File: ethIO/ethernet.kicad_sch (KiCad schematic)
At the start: 40 parts, among them J7 HR911130A1, U10 RTL8211E-VB-CG, Y1 25MHz

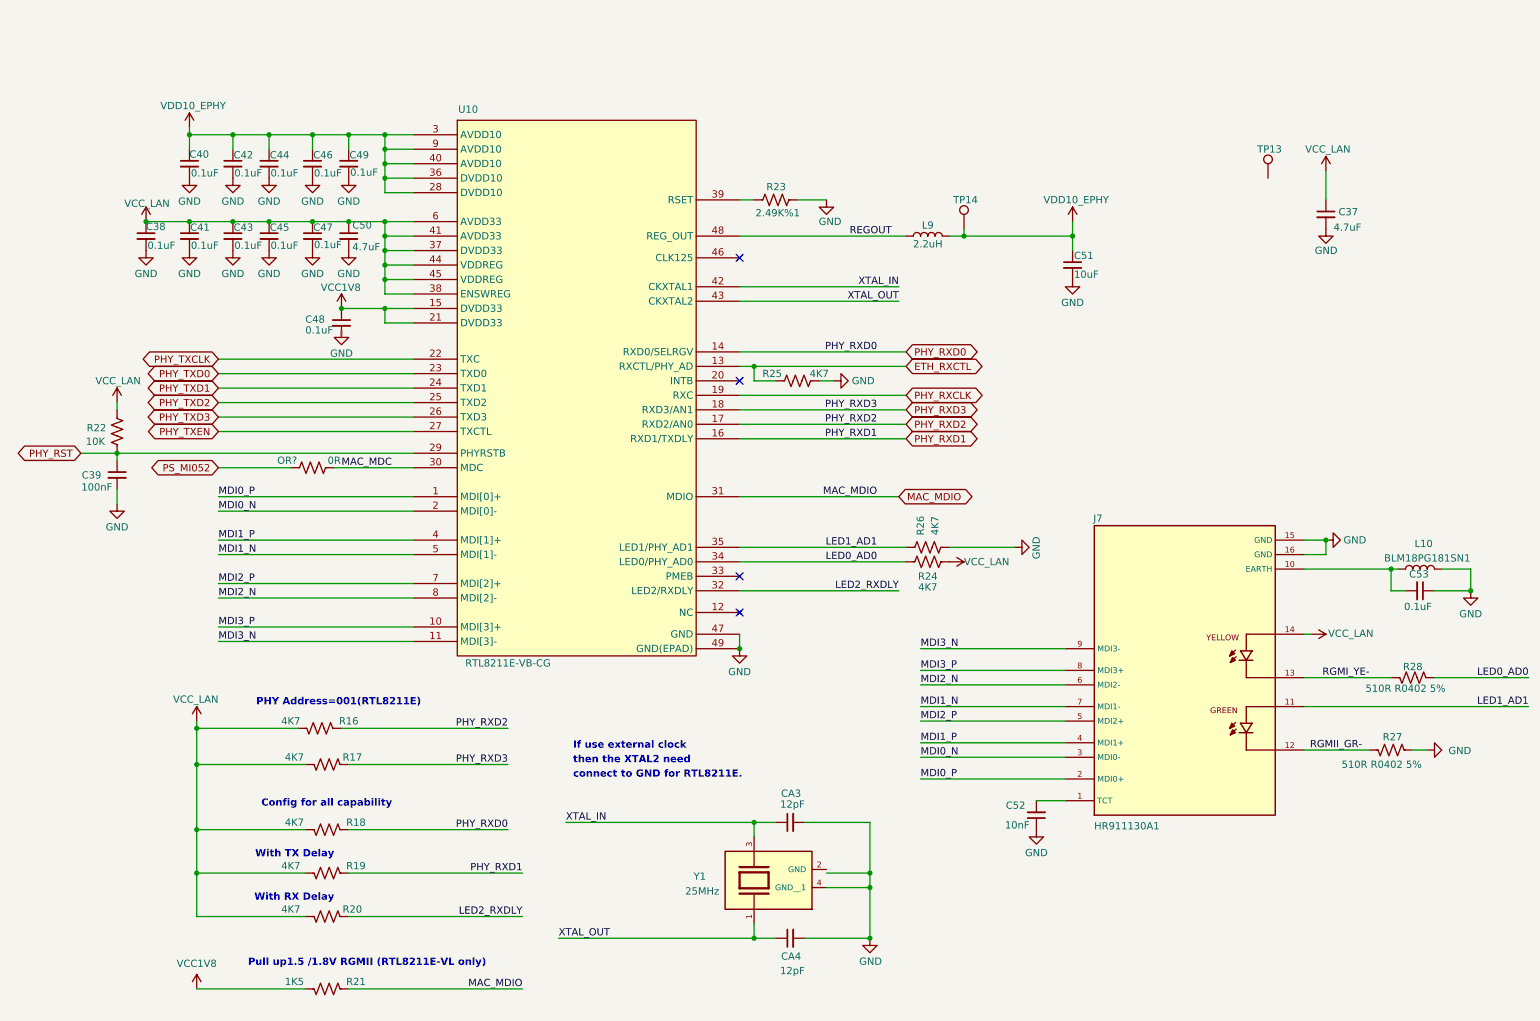
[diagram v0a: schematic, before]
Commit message: Updating ethIO
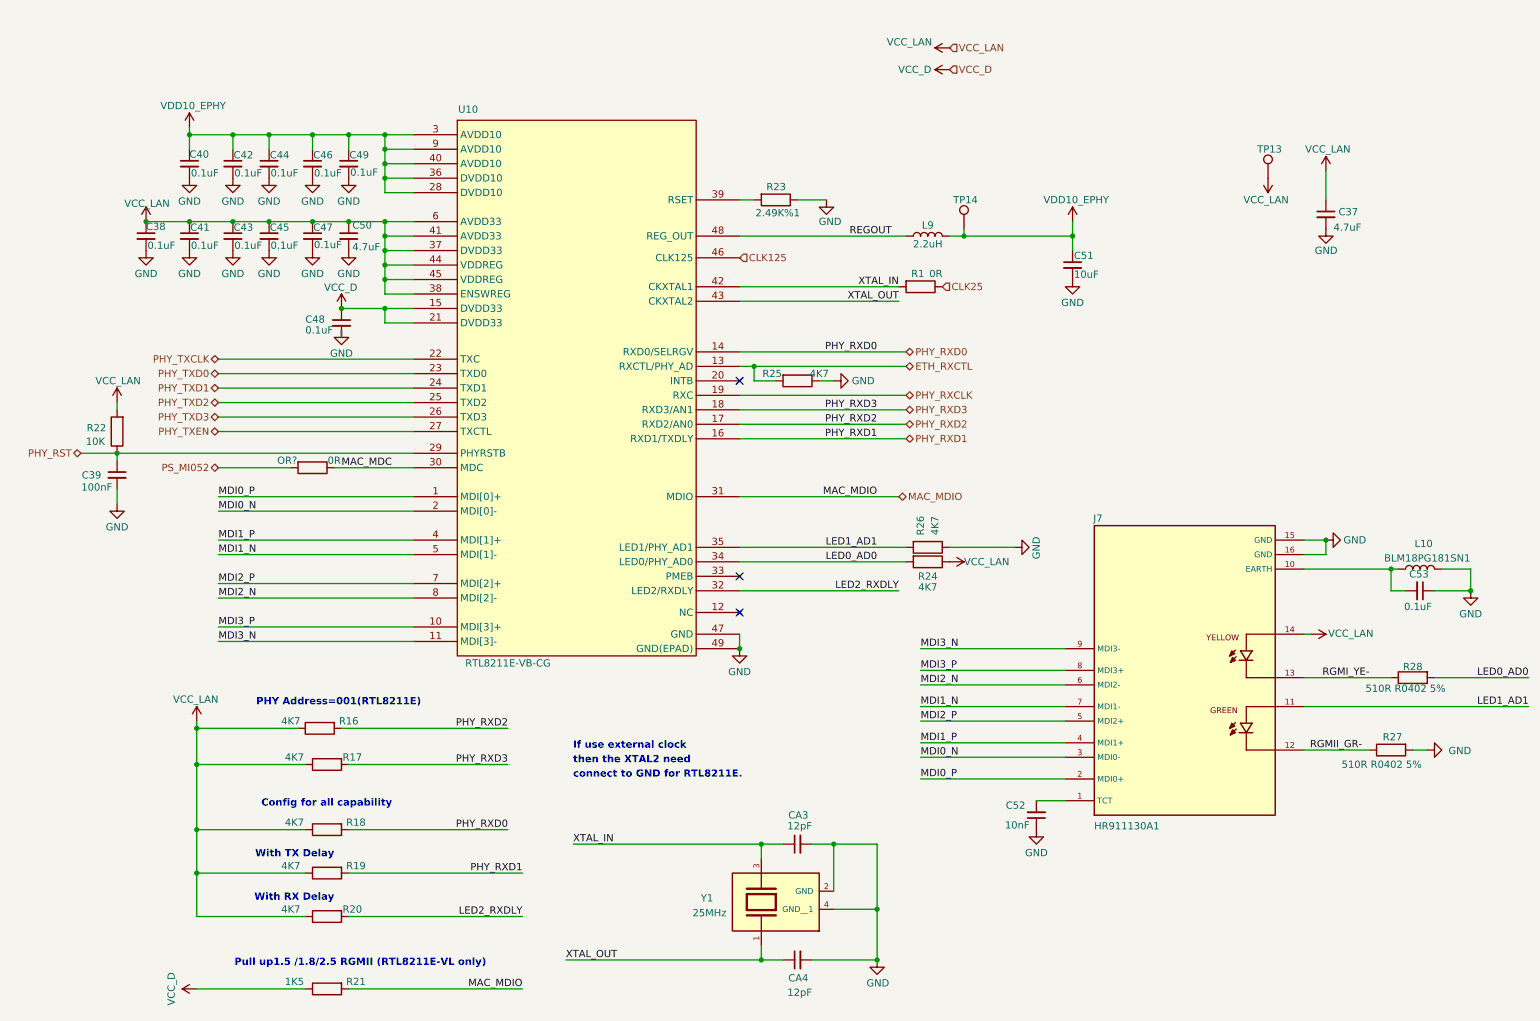
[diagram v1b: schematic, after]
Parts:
- added R1: 0R, Resistor_SMD:R_0402_1005Metric_Pad0.72x0.64mm_HandSolder, symbol Device:R
- J7: footprint Libraries:HR911130A_HAN -> HR911130A1:HR911130A_HAN
- OR?, R16, R17, R18, R19, R20, R21, R22, R23, R24, R25, R26, R27, R28: symbol Device:R_US -> Device:R
- U10: footprint Libraries:RTL8211E-VB-CG -> RTL8211E-VB-CG:RTL8211E-VB-CG
- Y1: footprint Libraries:XTAL_TSX-3225_25.0000MF10P-C0 -> Crystal:Crystal_SMD_SeikoEpson_TSX3225-4Pin_3.2x2.5mm
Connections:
- net GND: now also Y1.2 (GND)
- net VCC_LAN: now also TP13.1
- net XTAL_IN: now also R1.2
- net CLK125: now reaches U10.46 (CLK125)
- net VCC1V8 renamed VCC_D
- new net CLK25: R1.1
- no-connect marks 4 -> 3
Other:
- note added: "Pull up1.5 /1.8/2.5 RGMII (RTL8211E-VL only)"
- note removed: "Pull up1.5 /1.8V RGMII (RTL8211E-VL only)"
- moved on the sheet: CA3, CA4, Y1

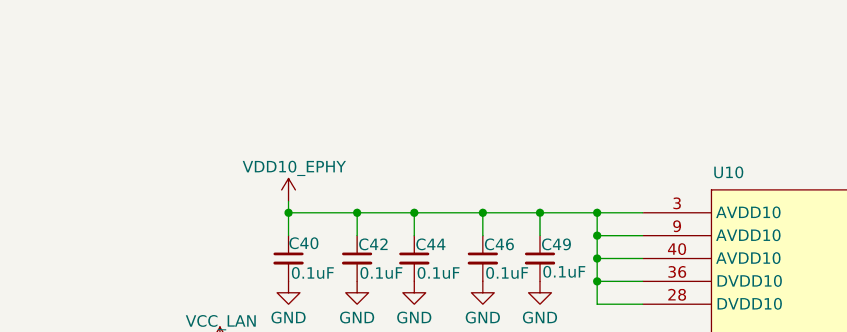
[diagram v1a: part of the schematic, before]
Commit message: Updating ethIO license
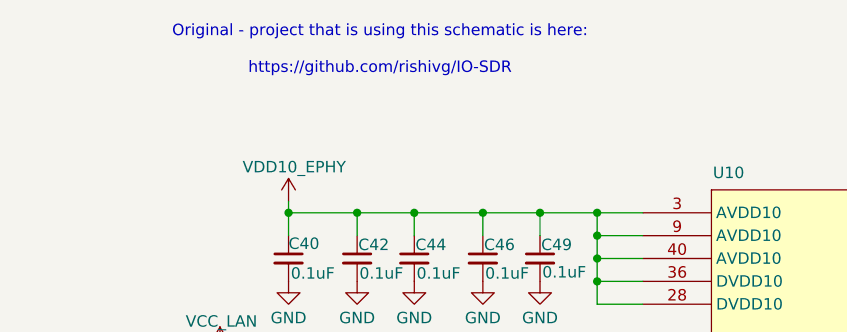
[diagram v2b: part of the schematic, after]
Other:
- note added: "Original - project that is using this schematic is here: https://github.com/rishivg/IO-SDR"
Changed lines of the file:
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@@
+		)
+	)
+	(text "Original - project that is using this schematic is here:\n\nhttps://github.com/rishivg/IO-SDR"
+		(exclude_from_sim no)
+		(at 52.07 17.526 0)
+		(effects
+			(font
+				(size 1.27 1.27)
+			)
 		)
 	)

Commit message: Moving to v9
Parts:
- gave numbers to parts that had none: 1
